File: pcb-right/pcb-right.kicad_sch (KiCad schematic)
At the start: 91 parts, among them J1 Conn_01x02_Pin, J2 Conn_01x06_MountingPin, J3 Conn_01x04_Pin, SW1 SW_Push, SW2 Rotary_Encoder_Default, U1 XC6206PxxxMR, U2 STM32F401RCTx, Y1 12MHz

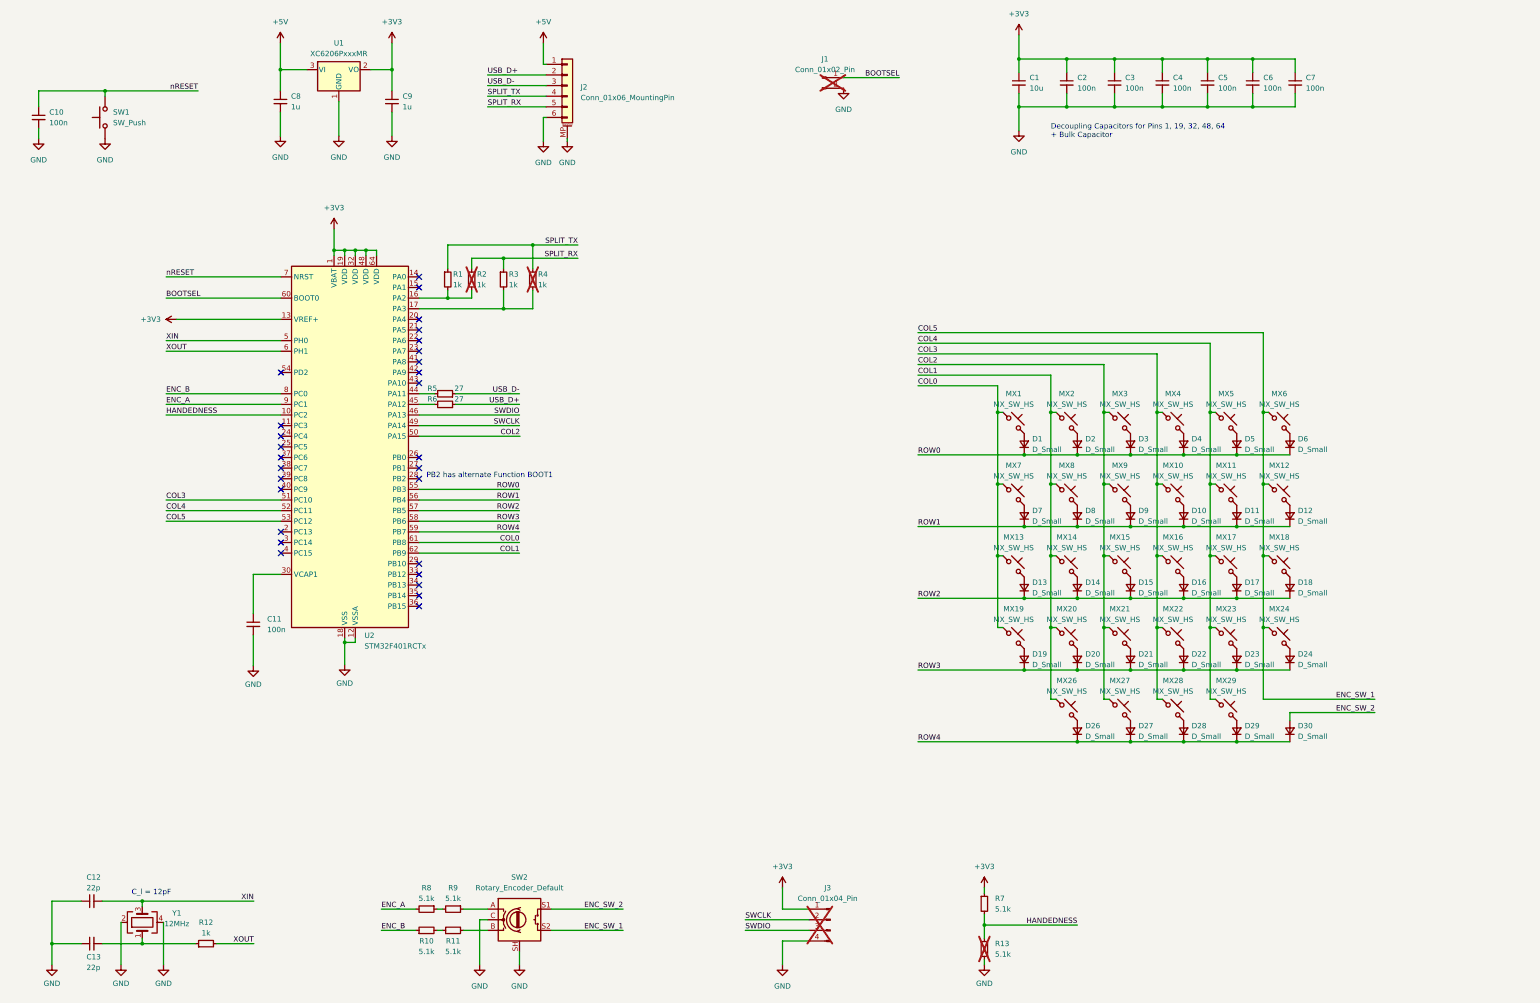
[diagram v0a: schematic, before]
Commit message: moved daughter board to separate projects for left and right halves fixed layouts of daughter boards..
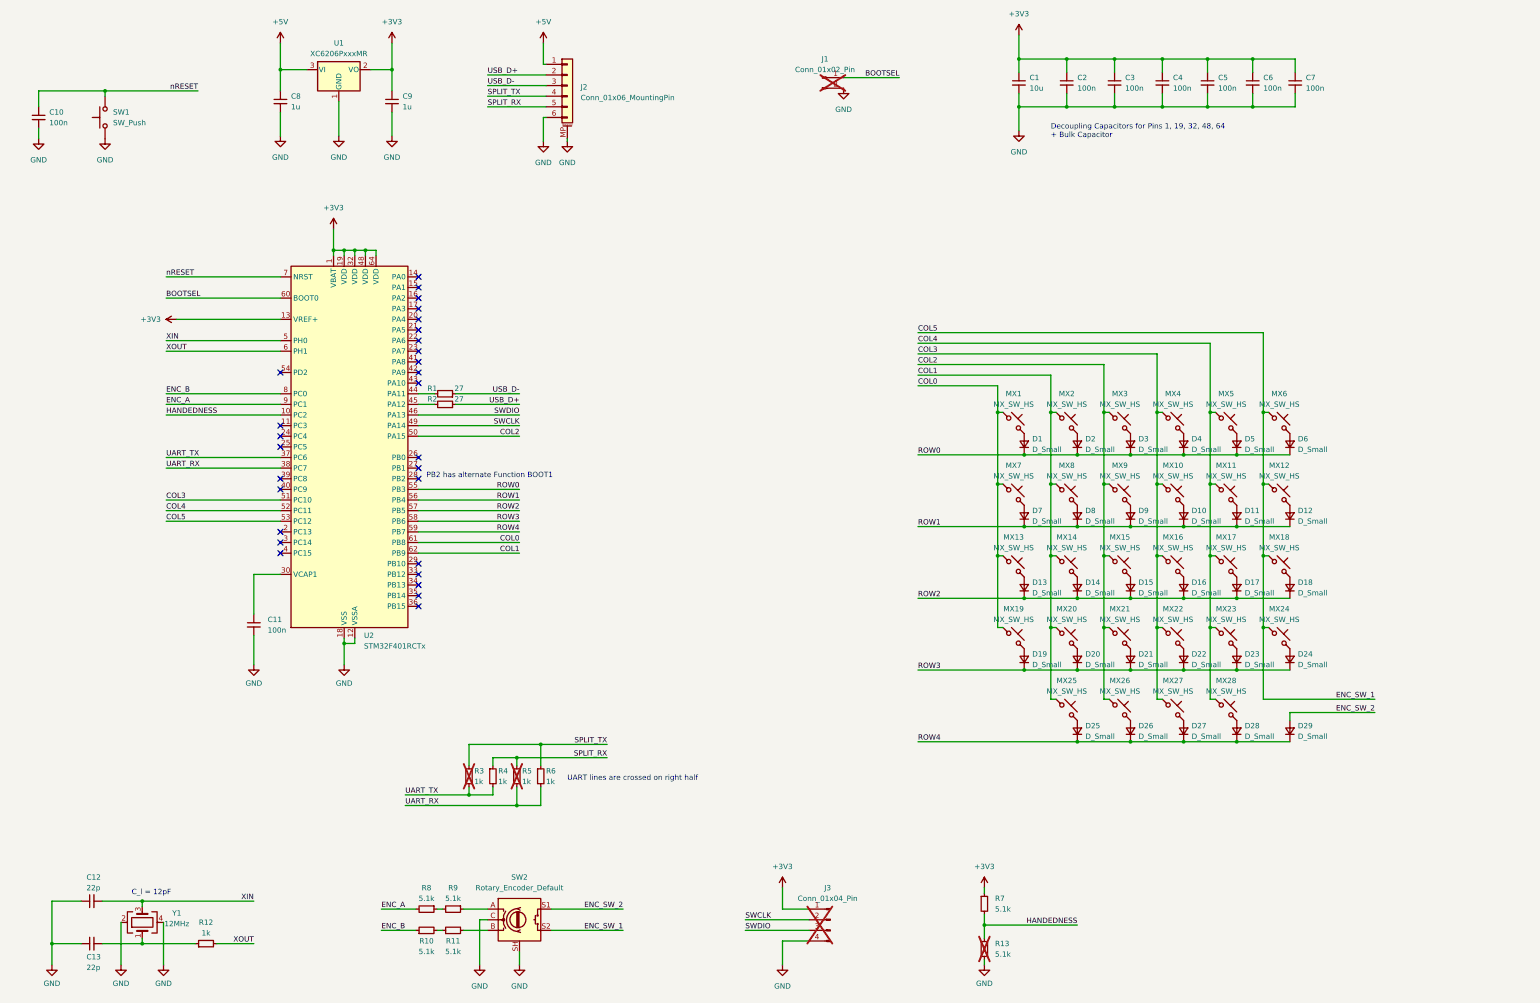
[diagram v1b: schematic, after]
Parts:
- C1, C10, C11, C12, C13, C2, C3, C4, C5, C6, C7, C8, C9: footprint Capacitor_SMD:C_0402_1005Metric -> Capacitor_SMD:C_0603_1608Metric
- R1: renamed from R5; footprint Resistor_SMD:R_0402_1005Metric -> Resistor_SMD:R_0603_1608Metric_Pad0.98x0.95mm_HandSolder
- R10, R11, R12, R13, R7, R8, R9: footprint Resistor_SMD:R_0402_1005Metric -> Resistor_SMD:R_0603_1608Metric_Pad0.98x0.95mm_HandSolder
- R2: renamed from R6; footprint Resistor_SMD:R_0402_1005Metric -> Resistor_SMD:R_0603_1608Metric_Pad0.98x0.95mm_HandSolder
- R3: renamed from R1; now not fitted; now left out of the parts list
- R4: renamed from R2; footprint Resistor_SMD:R_0402_1005Metric -> Resistor_SMD:R_0603_1608Metric_Pad0.98x0.95mm_HandSolder; now fitted
- R5: renamed from R3; now not fitted; now left out of the parts list
- R6: renamed from R4; footprint Resistor_SMD:R_0402_1005Metric -> Resistor_SMD:R_0603_1608Metric_Pad0.98x0.95mm_HandSolder; now fitted
- renumbered D26 to D25, D27 to D26, D28 to D27, D29 to D28, D30 to D29, MX26 to MX25, MX27 to MX26, MX28 to MX27, MX29 to MX28
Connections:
- net UART_RX: now reaches R5.2, R6.2
- net UART_RX: now also U2.38 (PC7); no longer U2.17 (PA3)
- net UART_TX: now reaches R3.2, R4.2
- net UART_TX: now also U2.37 (PC6); no longer U2.16 (PA2)
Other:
- note added: "UART lines are crossed on right half"

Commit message: quick save
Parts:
- removed R1, R2: 27, Resistor_SMD:R_0603_1608Metric_Pad0.98x0.95mm_HandSolder, symbol Device:R_Small
- removed R10, R8: 5.1k, Resistor_SMD:R_0603_1608Metric_Pad0.98x0.95mm_HandSolder, symbol Device:R_Small
- removed R12: 1k, Resistor_SMD:R_0603_1608Metric_Pad0.98x0.95mm_HandSolder, symbol Device:R_Small
- added C14: 100n, Capacitor_SMD:C_0603_1608Metric, symbol Device:C_Small
- added D30: ~, lib-zegonix:SK6812MINI-E_3.2x2.8_reverse_mount, symbol lib-zegonix:sk6812mini-e
- added R14, R15: 10k, Resistor_SMD:R_0603_1608Metric, symbol Device:R_Small
- C12, C13: value 22p -> 12p
- J2: footprint Connector_JST:JST_SHL_SM06B-SHLS-TF_1x06-1MP_P1.00mm_Horizontal -> Connector_JST:JST_SH_SM06B-SRSS-TB_1x06-1MP_P1.00mm_Horizontal
- R11, R9: value 5.1k -> 10K
- SW2: now not fitted; now left out of the parts list
- Y1: value 12MHz -> 8MHz
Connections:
- net +3V3: now also J1.1 (Pin_1), C14.1, D30.1 (VDD)
- net ENC_A: now also R9.2
- net ENC_B: now also R11.1
- net GND: now also C14.2, D30.3 (GND), R14.2, R15.2; no longer J1.2 (Pin_2)
- net USB_D+: now also U2.45 (PA12)
- net USB_D-: now also U2.44 (PA11)
- net XOUT: now also C13.2, Y1.1
- net BOOT1: now reaches U2.28 (PB2)
- net BOOT1: now also R15.1
- net IND_LED: now reaches U2.34 (PB13)
- net IND_LED: now also D30.4 (DIN)
- net BOOTSEL renamed BOOT0
- net BOOT0: now also J1.2 (Pin_2), R14.1; no longer J1.1 (Pin_1)
- no-connect marks 28 -> 27
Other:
- note added: "UART lines are crossed here on the right half"
- note removed: "C_l = 12pF"
- note removed: "PB2 has alternate Function BOOT1"
- note removed: "UART lines are crossed on right half"
- moved on the sheet: C1, C11, C12, C13, C2, C3, C4, C5, C6, C7, C8, C9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

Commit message: finalised first version of pcbs for prototype order added openscad file for the left halfs case
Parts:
- added D25: D_Small, Diode_SMD:D_SOD-123, symbol Device:D_Small
- added MX25: MX_SW_HS, PCM_marbastlib-mx:SW_MX_HS_1u, symbol PCM_marbastlib-mx:MX_SW_HS
- R10: renamed from R13; value 5.1k -> 10k
- R7: value 5.1k -> 10k
- renumbered C14 to C13, C13 to C14, D25 to D26, D26 to D27, D27 to D28, D28 to D29, D29 to D30, D30 to D31, J3 to J1, J1 to J2, J2 to J3, MX25 to MX26, MX26 to MX27, MX27 to MX28, MX28 to MX29, R14 to R1, R15 to R2, R9 to R8, R11 to R9
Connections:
- net COL0: now also U2.21 (PA5), MX25.1; no longer U2.61 (PB8)
- net COL1: now also U2.22 (PA6); no longer U2.62 (PB9)
- net COL2: now also U2.23 (PA7); no longer U2.50 (PA15)
- net COL3: now also U2.25 (PC5); no longer U2.51 (PC10)
- net COL4: now also U2.26 (PB0); no longer U2.52 (PC11)
- net COL5: now also U2.27 (PB1); no longer U2.53 (PC12)
- net ENC_A: now also U2.42 (PA9); no longer U2.9 (PC1)
- net ENC_B: now also U2.41 (PA8); no longer U2.8 (PC0)
- net HANDEDNESS: now also U2.16 (PA2); no longer U2.10 (PC2)
- net IND_LED: now also U2.15 (PA1); no longer U2.34 (PB13)
- net ROW0: now also U2.20 (PA4); no longer U2.55 (PB3)
- net ROW1: now also U2.24 (PC4); no longer U2.56 (PB4)
- net ROW2: now also U2.33 (PB12); no longer U2.57 (PB5)
- net ROW3: now also U2.34 (PB13); no longer U2.58 (PB6)
- net ROW4: now also U2.40 (PC9), D25.1 (K); no longer U2.59 (PB7)
- new net: D25.2 (A), MX25.2

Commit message: intermediate save
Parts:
- added R12: 1k, symbol Device:R_Small
- R3, R5: footprint Resistor_SMD:R_0402_1005Metric -> (none); now in the parts list
- R4, R6: footprint Resistor_SMD:R_0603_1608Metric_Pad0.98x0.95mm_HandSolder -> (none)
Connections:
- net COL0: now also U2.17 (PA3); no longer U2.21 (PA5)
- net COL1: now also U2.20 (PA4); no longer U2.22 (PA6)
- net COL2: now also U2.21 (PA5); no longer U2.23 (PA7)
- net COL3: now also U2.22 (PA6); no longer U2.25 (PC5)
- net COL4: now also U2.23 (PA7); no longer U2.26 (PB0)
- net COL5: now also U2.41 (PA8); no longer U2.27 (PB1)
- net ENC_A: now also U2.35 (PB14); no longer U2.42 (PA9)
- net ENC_B: now also U2.36 (PB15); no longer U2.41 (PA8)
- net GND: now also R12.2; no longer SW1.1
- net ROW0: now also U2.55 (PB3); no longer U2.20 (PA4)
- net ROW1: now also U2.56 (PB4); no longer U2.24 (PC4)
- net ROW2: now also U2.57 (PB5); no longer U2.33 (PB12)
- net ROW3: now also U2.58 (PB6); no longer U2.34 (PB13)
- net ROW4: now also U2.59 (PB7); no longer U2.40 (PC9)
- new net: R12.1, SW1.1
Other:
- moved on the sheet: C10, C11, SW1, U2
